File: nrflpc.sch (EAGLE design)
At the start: 74 parts, among them IC1 LPC1111/12/13/14-HVQFN33, IC2 LT1763CS8-3.3, IC3 LM3401, IC5 LM3401, IC6 LM3401, IC7 LM3401, Q1 20MHz, Q2 MOSFET-PCHANNEL, Q3 MOSFET-PCHANNEL, Q4 MOSFET-PCHANNEL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

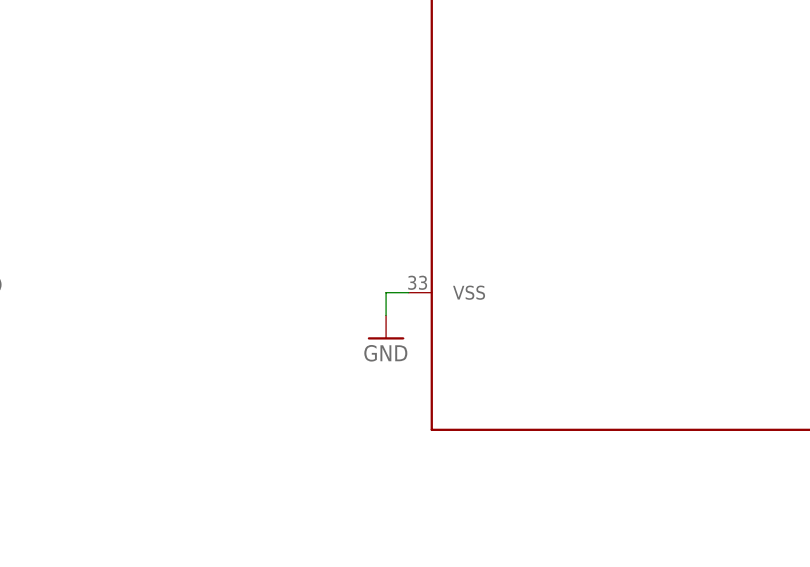
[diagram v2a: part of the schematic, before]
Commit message: updated HVQFN33 package
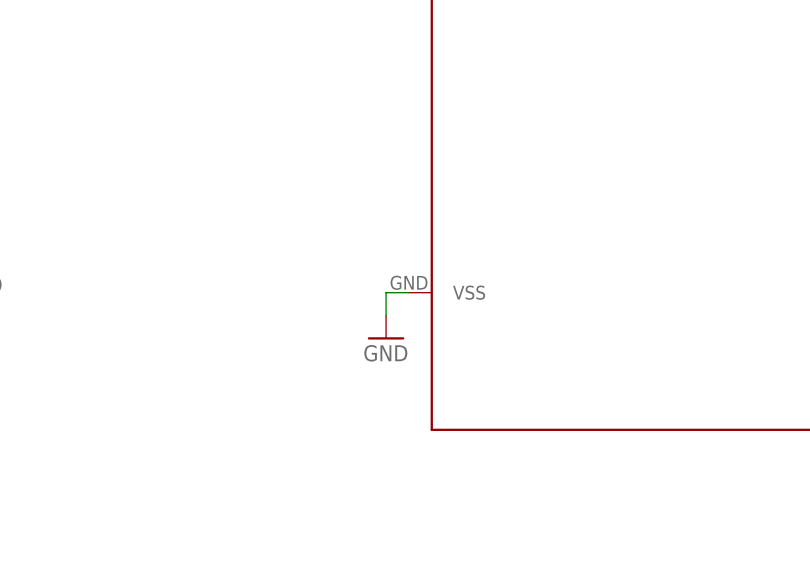
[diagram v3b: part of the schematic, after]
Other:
- moved on the sheet: IC1

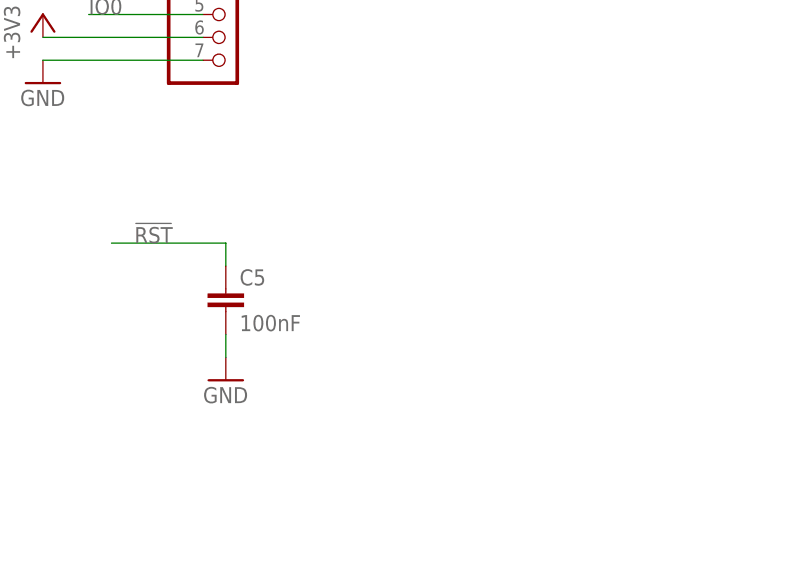
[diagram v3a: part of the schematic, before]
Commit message: Compacted right side, reset switch added
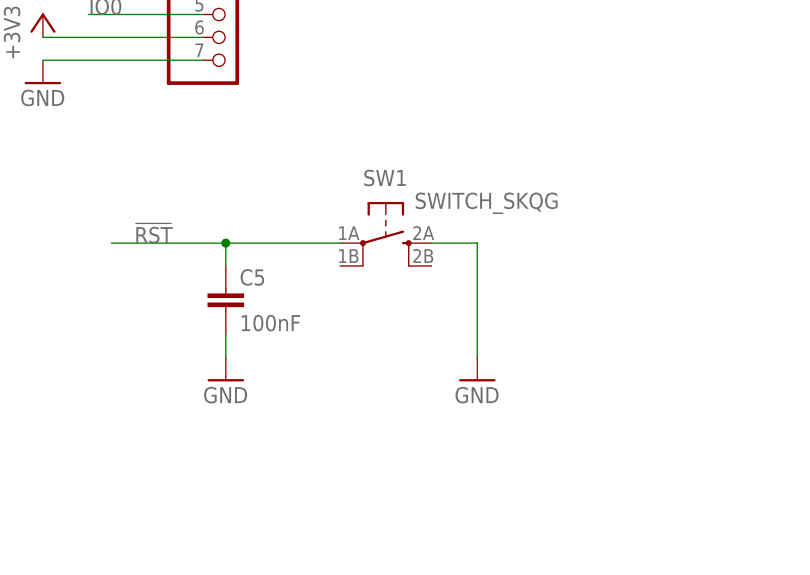
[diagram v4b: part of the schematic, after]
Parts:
- added SW1: SWITCH_SKQG, seb:SWITCH_SKQG
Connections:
- net !RST: now also SW1.1A
- net GND: now also SW1.2A
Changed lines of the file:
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@@
 <part name="R24" library="rcl" deviceset="R-US_" device="R0402" value="150"/>
 <part name="R25" library="rcl" deviceset="R-US_" device="R0402" value="150"/>
+<part name="SW1" library="seb" deviceset="SWITCH_SKQG" device=""/>
+<part name="GND17" library="supply1" deviceset="GND" device=""/>
 </parts>
 <sheets>
@@
 <instance part="R24" gate="G$1" x="246.38" y="187.96"/>
 <instance part="R25" gate="G$1" x="246.38" y="185.42"/>
+<instance part="SW1" gate="G$1" x="320.04" y="149.86"/>
+<instance part="GND17" gate="1" x="330.2" y="134.62"/>
 </instances>
 <busses>
@@
 <pinref part="GND16" gate="1" pin="GND"/>
 </segment>
+<segment>
+<pinref part="SW1" gate="G$1" pin="2A"/>
+<pinref part="GND17" gate="1" pin="GND"/>
+<wire x1="325.12" y1="149.86" x2="330.2" y2="149.86" width="0.1524" layer="91"/>
+<wire x1="330.2" y1="149.86" x2="330.2" y2="137.16" width="0.1524" layer="91"/>
+</segment>
 </net>
 <net name="!RST" class="0">
@@
 <wire x1="302.26" y1="149.86" x2="289.56" y2="149.86" width="0.1524" layer="91"/>
 <label x="292.1" y="149.86" size="1.778" layer="95"/>
-</segment>
-<segment>
+<pinref part="SW1" gate="G$1" pin="1A"/>
+<wire x1="314.96" y1="149.86" x2="302.26" y2="149.86" width="0.1524" layer="91"/>
+<junction x="302.26" y="149.86"/>
+</segment>
+<segment>

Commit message: Labels and Makeup
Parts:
- renumbered JP1 to NRF, SW1 to RESET
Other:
- moved on the sheet: R20
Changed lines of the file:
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@@
 <part name="FTDI" library="pinhead" deviceset="PINHD-1X6" device=""/>
 <part name="GND8" library="supply1" deviceset="GND" device=""/>
-<part name="JP1" library="pinhead" deviceset="PINHD-2X4" device=""/>
+<part name="NRF" library="pinhead" deviceset="PINHD-2X4" device=""/>
 <part name="+3V2" library="supply1" deviceset="+3V3" device=""/>
 <part name="GND3" library="supply1" deviceset="GND" device=""/>
@@
 <part name="R24" library="rcl" deviceset="R-US_" device="R0402" value="150"/>
 <part name="R25" library="rcl" deviceset="R-US_" device="R0402" value="150"/>
-<part name="SW1" library="seb" deviceset="SWITCH_SKQG" device=""/>
+<part name="RESET" library="seb" deviceset="SWITCH_SKQG" device=""/>
 <part name="GND17" library="supply1" deviceset="GND" device=""/>
 </parts>
@@
 <instance part="FTDI" gate="A" x="88.9" y="144.78"/>
 <instance part="GND8" gate="1" x="73.66" y="134.62"/>
-<instance part="JP1" gate="A" x="106.68" y="93.98" rot="R180"/>
+<instance part="NRF" gate="A" x="106.68" y="93.98" rot="R180"/>
 <instance part="+3V2" gate="G$1" x="83.82" y="91.44"/>
 <instance part="GND3" gate="1" x="127" y="86.36"/>
@@
 <instance part="R19" gate="G$1" x="375.92" y="109.22" rot="R180"/>
 <instance part="GND15" gate="1" x="365.76" y="93.98"/>
-<instance part="R20" gate="G$1" x="238.76" y="149.86"/>
+<instance part="R20" gate="G$1" x="241.3" y="149.86"/>
 <instance part="R21" gate="G$1" x="238.76" y="147.32"/>
 <instance part="IC2" gate="G$1" x="208.28" y="45.72"/>
@@
 <instance part="R24" gate="G$1" x="246.38" y="187.96"/>
 <instance part="R25" gate="G$1" x="246.38" y="185.42"/>
-<instance part="SW1" gate="G$1" x="320.04" y="149.86"/>
+<instance part="RESET" gate="G$1" x="320.04" y="149.86"/>
 <instance part="GND17" gate="1" x="330.2" y="134.62"/>
 </instances>
@@
 </segment>
 <segment>
-<pinref part="JP1" gate="A" pin="1"/>
+<pinref part="NRF" gate="A" pin="1"/>
 <wire x1="109.22" y1="88.9" x2="124.46" y2="88.9" width="0.1524" layer="91"/>
 <pinref part="GND3" gate="1" pin="GND"/>
@@
 </segment>
 <segment>
-<pinref part="SW1" gate="G$1" pin="2A"/>
+<pinref part="RESET" gate="G$1" pin="2A"/>
 <pinref part="GND17" gate="1" pin="GND"/>
 <wire x1="325.12" y1="149.86" x2="330.2" y2="149.86" width="0.1524" layer="91"/>
@@
 <wire x1="302.26" y1="149.86" x2="289.56" y2="149.86" width="0.1524" layer="91"/>
 <label x="292.1" y="149.86" size="1.778" layer="95"/>
-<pinref part="SW1" gate="G$1" pin="1A"/>
+<pinref part="RESET" gate="G$1" pin="1A"/>
 <wire x1="314.96" y1="149.86" x2="302.26" y2="149.86" width="0.1524" layer="91"/>
 <junction x="302.26" y="149.86"/>
@@
 <segment>
 <pinref part="R20" gate="G$1" pin="2"/>
-<wire x1="243.84" y1="149.86" x2="254" y2="149.86" width="0.1524" layer="91"/>
+<wire x1="246.38" y1="149.86" x2="254" y2="149.86" width="0.1524" layer="91"/>
 <label x="248.92" y="149.86" size="1.778" layer="95"/>
 </segment>
@@
 </segment>
 <segment>
-<pinref part="JP1" gate="A" pin="2"/>
+<pinref part="NRF" gate="A" pin="2"/>
 <wire x1="101.6" y1="88.9" x2="83.82" y2="88.9" width="0.1524" layer="91"/>
 <pinref part="+3V2" gate="G$1" pin="+3V3"/>
@@
 <net name="CE" class="0">
 <segment>
-<pinref part="JP1" gate="A" pin="3"/>
+<pinref part="NRF" gate="A" pin="3"/>
 <wire x1="109.22" y1="91.44" x2="124.46" y2="91.44" width="0.1524" layer="91"/>
 <label x="124.46" y="91.44" size="1.778" layer="95"/>
@@
 <net name="SCK" class="0">
 <segment>
-<pinref part="JP1" gate="A" pin="5"/>
+<pinref part="NRF" gate="A" pin="5"/>
 <wire x1="109.22" y1="93.98" x2="124.46" y2="93.98" width="0.1524" layer="91"/>
 <label x="124.46" y="93.98" size="1.778" layer="95"/>
@@
 <net name="MISO" class="0">
 <segment>
-<pinref part="JP1" gate="A" pin="7"/>
+<pinref part="NRF" gate="A" pin="7"/>
 <wire x1="109.22" y1="96.52" x2="124.46" y2="96.52" width="0.1524" layer="91"/>
 <label x="124.46" y="96.52" size="1.778" layer="95"/>
@@
 <net name="IRQ" class="0">
 <segment>
-<pinref part="JP1" gate="A" pin="8"/>
+<pinref part="NRF" gate="A" pin="8"/>
 <wire x1="101.6" y1="96.52" x2="86.36" y2="96.52" width="0.1524" layer="91"/>
 <label x="86.36" y="96.52" size="1.778" layer="95"/>
@@
 <net name="MOSI" class="0">
 <segment>
-<pinref part="JP1" gate="A" pin="6"/>
+<pinref part="NRF" gate="A" pin="6"/>
 <wire x1="101.6" y1="93.98" x2="86.36" y2="93.98" width="0.1524" layer="91"/>
 <label x="86.36" y="93.98" size="1.778" layer="95"/>
@@
 <net name="CSN" class="0">
 <segment>
-<pinref part="JP1" gate="A" pin="4"/>
+<pinref part="NRF" gate="A" pin="4"/>
 <wire x1="101.6" y1="91.44" x2="86.36" y2="91.44" width="0.1524" layer="91"/>
 <label x="86.36" y="91.44" size="1.778" layer="95"/>
@@
 <pinref part="IC1" gate="G$1" pin="PIO1_6/RXD/CT32B0_MAT0"/>
 <pinref part="R20" gate="G$1" pin="1"/>
-<wire x1="231.14" y1="149.86" x2="233.68" y2="149.86" width="0.1524" layer="91"/>
-</segment>
-</net>
+<wire x1="231.14" y1="149.86" x2="236.22" y2="149.86" width="0.1524" layer="91"/>
+</segment>
+</net>

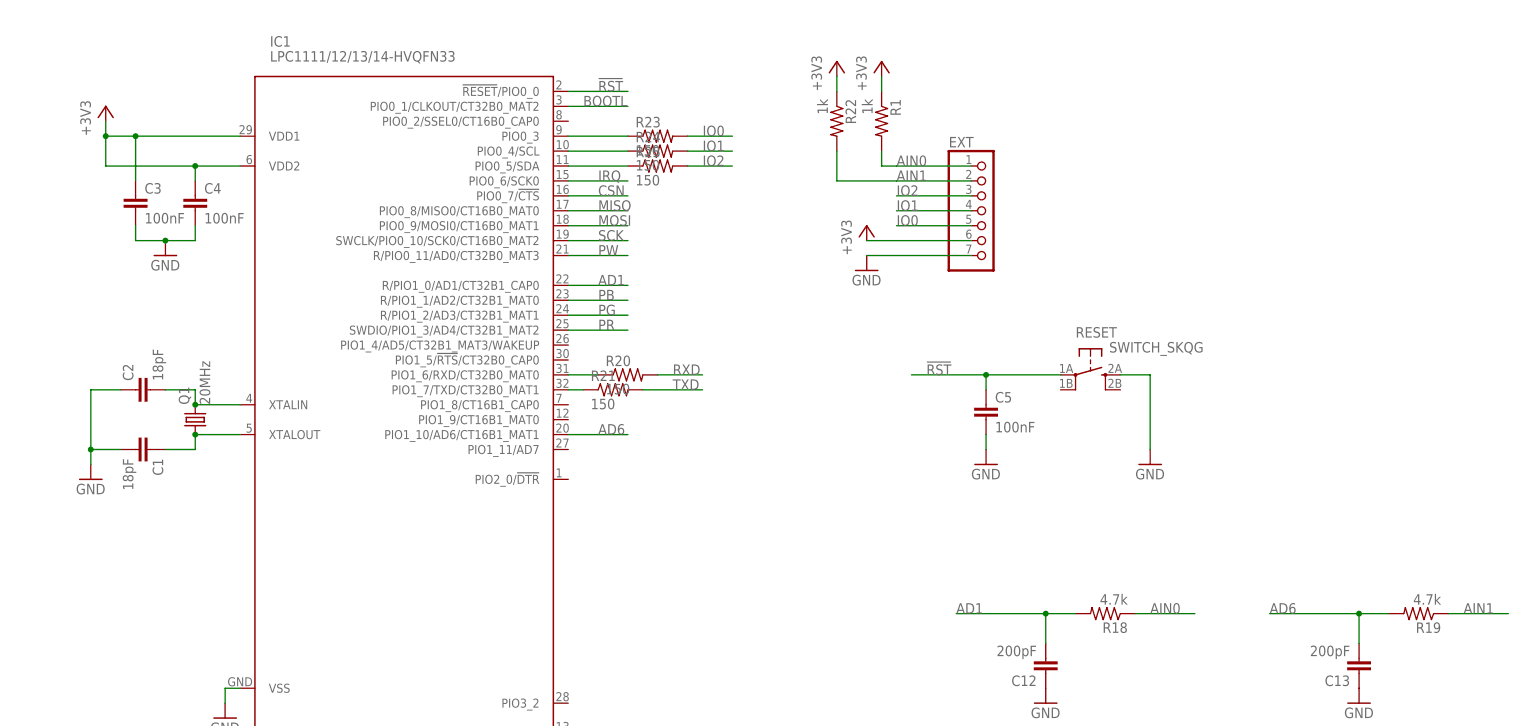
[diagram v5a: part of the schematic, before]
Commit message: More silkscreen
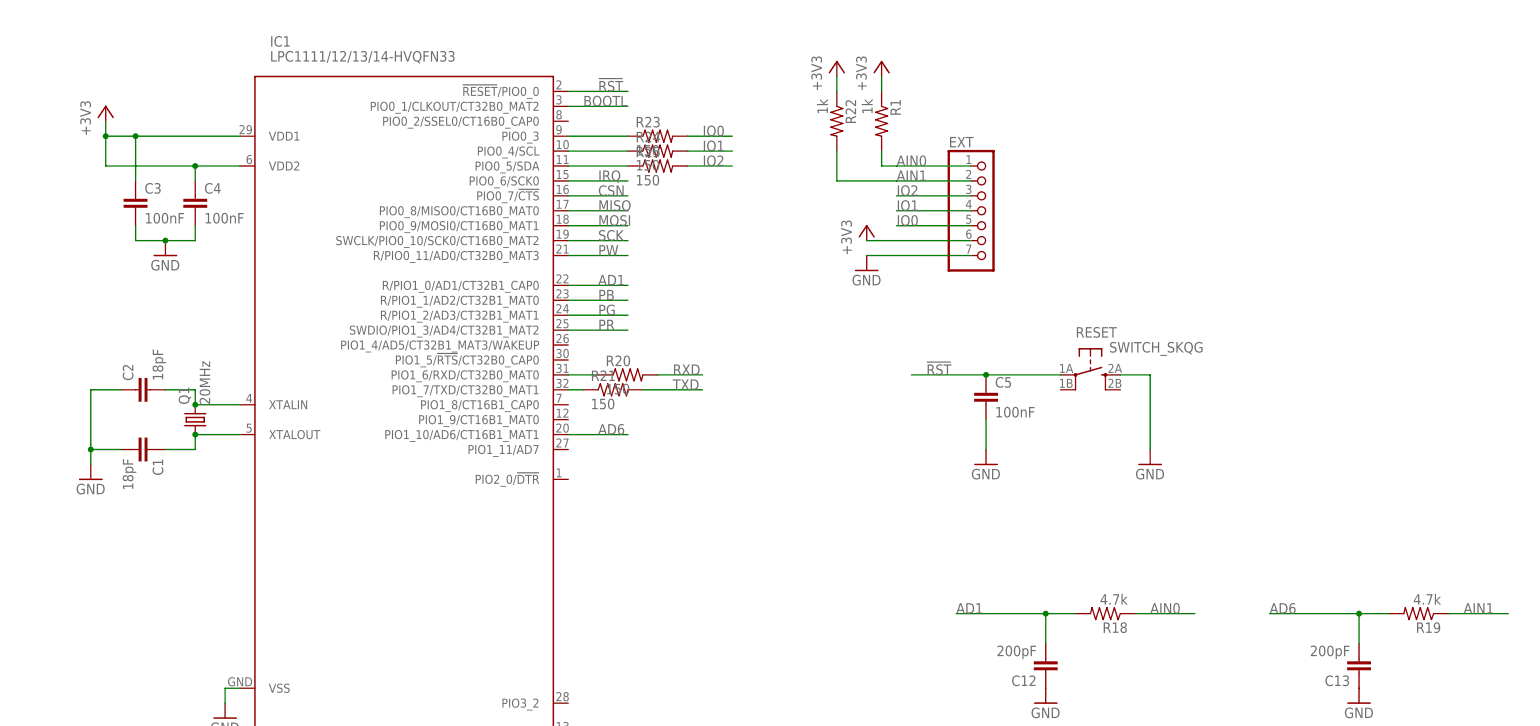
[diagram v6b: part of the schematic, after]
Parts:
- C1, C2, C3, C4, C5: device rcl:C-EUC0402 -> SparkFun-Passives:CAP0402-CAP
- C12, C13: device SparkFun:CAP0402-CAP -> SparkFun-Passives:CAP0402-CAP
- R1, R18, R19, R20, R21, R22, R23, R24, R25: device rcl:R-US_R0402 -> SparkFun-Resistors:RESISTOR0402-RES
- R2, R3, R4, R5: device SparkFun:RESISTOR0402-RES -> SparkFun-Resistors:RESISTOR0402-RES
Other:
- moved on the sheet: C5
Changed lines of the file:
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@@
 </classes>
 <parts>
-<part name="R4" library="SparkFun" deviceset="RESISTOR" device="0402-RES" value="100K"/>
-<part name="R3" library="SparkFun" deviceset="RESISTOR" device="0402-RES" value="100K"/>
-<part name="R2" library="SparkFun" deviceset="RESISTOR" device="0402-RES" value="100K"/>
+<part name="R4" library="SparkFun-Resistors" deviceset="RESISTOR" device="0402-RES" value="100K"/>
+<part name="R3" library="SparkFun-Resistors" deviceset="RESISTOR" device="0402-RES" value="100K"/>
+<part name="R2" library="SparkFun-Resistors" deviceset="RESISTOR" device="0402-RES" value="100K"/>
 <part name="GND7" library="supply1" deviceset="GND" device=""/>
 <part name="W+" library="solpad" deviceset="SE14" device=""/>
-<part name="R5" library="SparkFun" deviceset="RESISTOR" device="0402-RES" value="100K"/>
+<part name="R5" library="SparkFun-Resistors" deviceset="RESISTOR" device="0402-RES" value="100K"/>
 <part name="P+6" library="supply1" deviceset="+12V" device=""/>
 <part name="IC3" library="seb" deviceset="LM3401" device=""/>
@@
 <part name="IC1" library="lpc1100v1.1" deviceset="LPC1111/12/13/14-HVQFN33" device=""/>
 <part name="Q1" library="seb" deviceset="MT-OSCILLATOR" device="" value="20MHz"/>
-<part name="C1" library="rcl" deviceset="C-EU" device="C0402" value="18pF"/>
-<part name="C2" library="rcl" deviceset="C-EU" device="C0402" value="18pF"/>
+<part name="C1" library="SparkFun-Passives" deviceset="CAP" device="0402-CAP" value="18pF"/>
+<part name="C2" library="SparkFun-Passives" deviceset="CAP" device="0402-CAP" value="18pF"/>
 <part name="GND1" library="supply1" deviceset="GND" device=""/>
 <part name="GND2" library="supply1" deviceset="GND" device=""/>
 <part name="+3V4" library="supply1" deviceset="+3V3" device=""/>
-<part name="C3" library="rcl" deviceset="C-EU" device="C0402" value="100nF"/>
-<part name="C4" library="rcl" deviceset="C-EU" device="C0402" value="100nF"/>
+<part name="C3" library="SparkFun-Passives" deviceset="CAP" device="0402-CAP" value="100nF"/>
+<part name="C4" library="SparkFun-Passives" deviceset="CAP" device="0402-CAP" value="100nF"/>
 <part name="GND5" library="supply1" deviceset="GND" device=""/>
 <part name="GND13" library="supply1" deviceset="GND" device=""/>
-<part name="C5" library="rcl" deviceset="C-EU" device="C0402" value="100nF"/>
+<part name="C5" library="SparkFun-Passives" deviceset="CAP" device="0402-CAP" value="100nF"/>
 <part name="PWR" library="pinhead" deviceset="PINHD-1X2" device=""/>
 <part name="P+1" library="supply1" deviceset="+12V" device=""/>
 <part name="GND12" library="supply1" deviceset="GND" device=""/>
-<part name="C12" library="SparkFun" deviceset="CAP" device="0402-CAP" value="200pF"/>
-<part name="R18" library="rcl" deviceset="R-US_" device="R0402" value="4.7k"/>
+<part name="C12" library="SparkFun-Passives" deviceset="CAP" device="0402-CAP" value="200pF"/>
+<part name="R18" library="SparkFun-Resistors" deviceset="RESISTOR" device="0402-RES" value="4.7k"/>
 <part name="GND14" library="supply1" deviceset="GND" device=""/>
-<part name="C13" library="SparkFun" deviceset="CAP" device="0402-CAP" value="200pF"/>
-<part name="R19" library="rcl" deviceset="R-US_" device="R0402" value="4.7k"/>
+<part name="C13" library="SparkFun-Passives" deviceset="CAP" device="0402-CAP" value="200pF"/>
+<part name="R19" library="SparkFun-Resistors" deviceset="RESISTOR" device="0402-RES" value="4.7k"/>
 <part name="GND15" library="supply1" deviceset="GND" device=""/>
-<part name="R20" library="rcl" deviceset="R-US_" device="R0402" value="150"/>
-<part name="R21" library="rcl" deviceset="R-US_" device="R0402" value="150"/>
+<part name="R20" library="SparkFun-Resistors" deviceset="RESISTOR" device="0402-RES" value="150"/>
+<part name="R21" library="SparkFun-Resistors" deviceset="RESISTOR" device="0402-RES" value="150"/>
 <part name="IC2" library="linear-technology" deviceset="LT1763CS8" device="" technology="-3.3"/>
 <part name="C18" library="SparkFun" deviceset="CAP" device="0402-CAP" value="10nF"/>
@@
 <part name="GND16" library="supply1" deviceset="GND" device=""/>
 <part name="+3V3" library="supply1" deviceset="+3V3" device=""/>
-<part name="R1" library="rcl" deviceset="R-US_" device="R0402" value="1k"/>
-<part name="R22" library="rcl" deviceset="R-US_" device="R0402" value="1k"/>
+<part name="R1" library="SparkFun-Resistors" deviceset="RESISTOR" device="0402-RES" value="1k"/>
+<part name="R22" library="SparkFun-Resistors" deviceset="RESISTOR" device="0402-RES" value="1k"/>
 <part name="+3V5" library="supply1" deviceset="+3V3" device=""/>
 <part name="+3V6" library="supply1" deviceset="+3V3" device=""/>
-<part name="R23" library="rcl" deviceset="R-US_" device="R0402" value="150"/>
-<part name="R24" library="rcl" deviceset="R-US_" device="R0402" value="150"/>
-<part name="R25" library="rcl" deviceset="R-US_" device="R0402" value="150"/>
+<part name="R23" library="SparkFun-Resistors" deviceset="RESISTOR" device="0402-RES" value="150"/>
+<part name="R24" library="SparkFun-Resistors" deviceset="RESISTOR" device="0402-RES" value="150"/>
+<part name="R25" library="SparkFun-Resistors" deviceset="RESISTOR" device="0402-RES" value="150"/>
 <part name="RESET" library="seb" deviceset="SWITCH_SKQG" device=""/>
 <part name="GND17" library="supply1" deviceset="GND" device=""/>
@@
 <instance part="IC1" gate="G$1" x="203.2" y="142.24"/>
 <instance part="Q1" gate="G$1" x="167.64" y="142.24" rot="R90"/>
-<instance part="C1" gate="G$1" x="160.02" y="137.16" rot="R270"/>
-<instance part="C2" gate="G$1" x="157.48" y="147.32" rot="R90"/>
+<instance part="C1" gate="G$1" x="157.48" y="137.16" rot="R270"/>
+<instance part="C2" gate="G$1" x="160.02" y="147.32" rot="R90"/>
 <instance part="GND1" gate="1" x="149.86" y="132.08"/>
 <instance part="GND2" gate="1" x="172.72" y="91.44"/>
 <instance part="+3V4" gate="G$1" x="152.4" y="195.58"/>
-<instance part="C3" gate="G$1" x="157.48" y="180.34"/>
-<instance part="C4" gate="G$1" x="167.64" y="180.34"/>
+<instance part="C3" gate="G$1" x="157.48" y="177.8"/>
+<instance part="C4" gate="G$1" x="167.64" y="177.8"/>
 <instance part="GND5" gate="1" x="162.56" y="170.18"/>
 <instance part="GND13" gate="1" x="302.26" y="134.62"/>
@@
 <pinref part="C5" gate="G$1" pin="2"/>
 <pinref part="GND13" gate="1" pin="GND"/>
-<wire x1="302.26" y1="139.7" x2="302.26" y2="137.16" width="0.1524" layer="91"/>
+<wire x1="302.26" y1="142.24" x2="302.26" y2="137.16" width="0.1524" layer="91"/>
 </segment>
 <segment>
@@
 <segment>
 <pinref part="C5" gate="G$1" pin="1"/>
-<wire x1="302.26" y1="147.32" x2="302.26" y2="149.86" width="0.1524" layer="91"/>
 <wire x1="302.26" y1="149.86" x2="289.56" y2="149.86" width="0.1524" layer="91"/>
 <label x="292.1" y="149.86" size="1.778" layer="95"/>
@@
 <wire x1="152.4" y1="190.5" x2="152.4" y2="193.04" width="0.1524" layer="91"/>
 <pinref part="IC1" gate="G$1" pin="VDD2"/>
-<wire x1="175.26" y1="185.42" x2="167.64" y2="185.42" width="0.1524" layer="91"/>
-<wire x1="167.64" y1="185.42" x2="152.4" y2="185.42" width="0.1524" layer="91"/>
 <wire x1="152.4" y1="185.42" x2="152.4" y2="190.5" width="0.1524" layer="91"/>
 <junction x="152.4" y="190.5"/>
@@
 <junction x="157.48" y="190.5"/>
 <pinref part="C4" gate="G$1" pin="1"/>
+<wire x1="152.4" y1="185.42" x2="167.64" y2="185.42" width="0.1524" layer="91"/>
+<wire x1="167.64" y1="185.42" x2="175.26" y2="185.42" width="0.1524" layer="91"/>
 <wire x1="167.64" y1="182.88" x2="167.64" y2="185.42" width="0.1524" layer="91"/>
 <junction x="167.64" y="185.42"/>
